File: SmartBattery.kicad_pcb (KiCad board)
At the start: 4 copper layers, 100 x 70 mm, 320 parts, among them J1 USB_C_Receptacle_USB2.0, J10 JST 2P-1.0, J11 JST 2P-1.0, J15 USB_C_Receptacle_USB2.0, J2 ST-USB-003A, J3 Barrel_Jack_MountingPin, J4 JST 2P-1.0, J5 JST 2P-1.0, J6 JST 2P-1.0, J7 JST 2P-1.0, J8 JST 2P-1.0, J9 JST 2P-1.0, Q1 VBA2625, Q10 AON7400A, Q11 AON7400A, Q12 AON7400A, Q13 AON7400A, Q14 2n7002K, Q15 VBA2625, Q16 VBA2625, Q17 VBA2625, Q18 VBA2625, Q19 VBA2625, Q2 2n7002K, Q20 VBA2625, Q21 2n7002K, Q22 VBA2625, Q23 2n7002K, Q24 VBA2625, Q3 AON7400A, Q4 AON7400A, Q5 AON7400A, Q6 AON7400A, Q7 2n7002K, Q8 AON7400A, Q9 AON7400A, SW1 SW_Push, SW2 SW_Push, U1 BQ25703ARSNR, U10 ESP32-WROOM-32U, U11 STUSB4500, U12 STUSB4700, U13 TPS2511DGNR, U2 BQ294706DSGR, U3 ITV4030, U4 BQ40Z50, U5 LM5175PWPR, U6 STM32F730R8T6, U7 W25Q128JVSIQ, U8 LMR14030SDDAR, U9 FS35ND01G-S1Y2QWFI000, Y1 Q13FC1350000400, Y2 Crystal_GND24

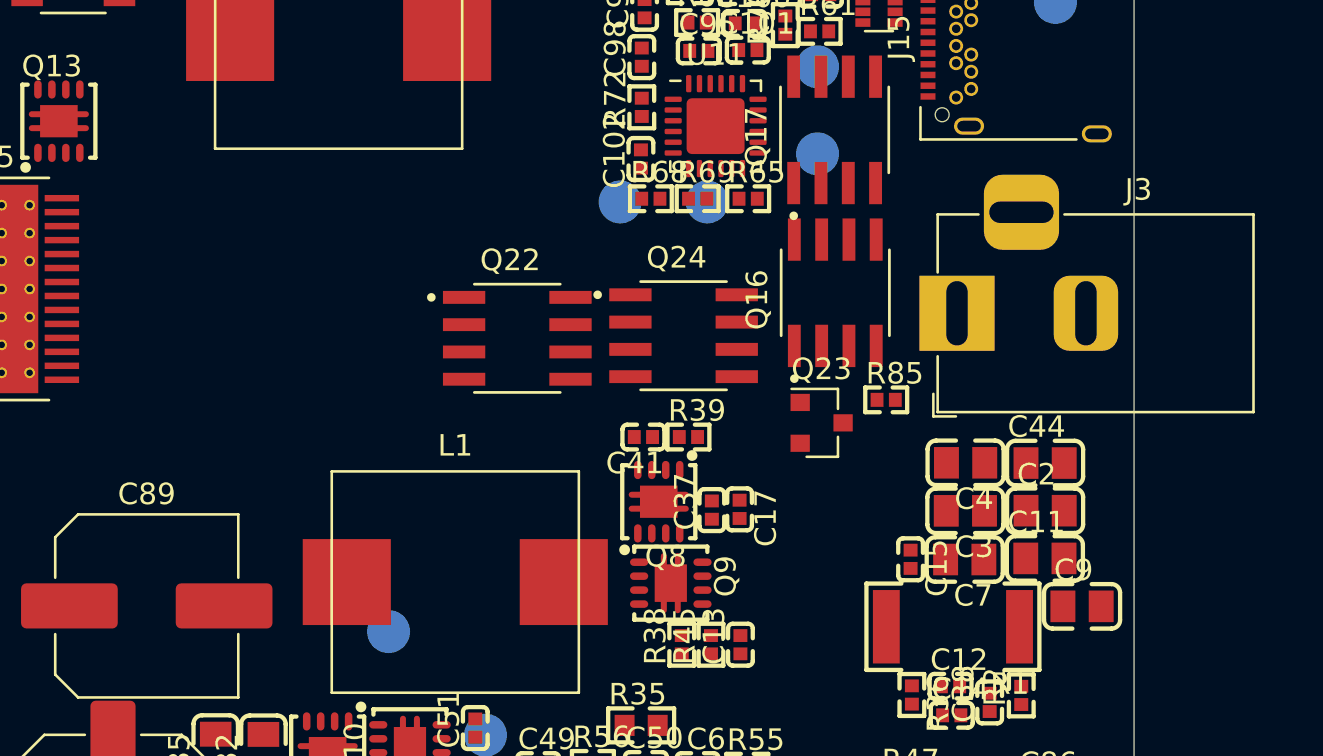
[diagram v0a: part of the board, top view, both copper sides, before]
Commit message: Added final touches to barrel jack and feedforward.
Need to finish output stage, then add screw terminals.
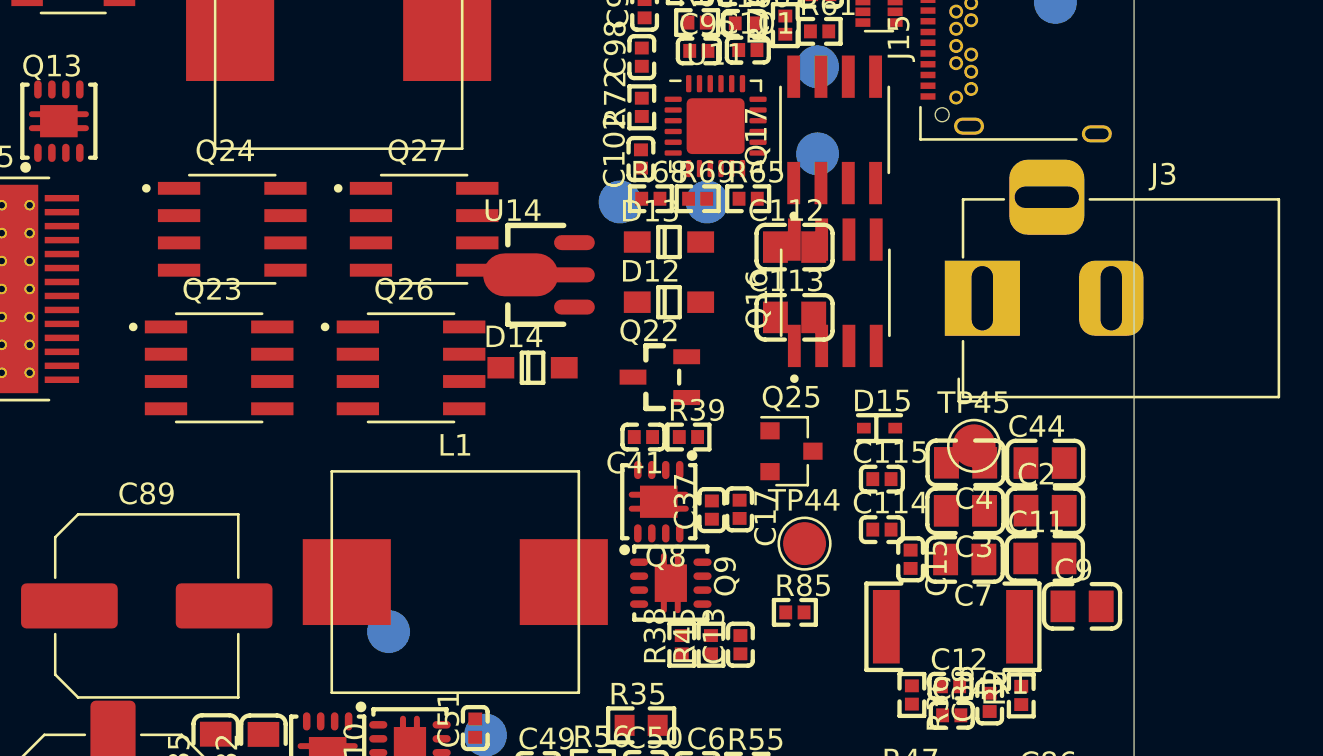
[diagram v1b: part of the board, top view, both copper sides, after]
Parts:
- added C112: 10u, lc_lib:0805_C, F.Cu at (84.2, 15.3)
- added C113: 10u, lc_lib:0805_C, F.Cu at (84.2, 18.6)
- added C114: 1uF 25v, lc_lib:0402_C, F.Cu at (88.3, 28.5)
- added C115: 1uF 25v, lc_lib:0402_C, F.Cu at (88.3, 26.1)
- added D12: B5817W-5819W, lc_lib:SOD-123, F.Cu at (78.4, 17.9)
- added D13: B5817W-5819W, lc_lib:SOD-123, F.Cu at (78.4, 15.1)
- added D14: B5817W-5819W, lc_lib:SOD-123, F.Cu at (72.0, 20.9)
- added D15: PESD24VS1UB-N, lc_lib:SOD-523, F.Cu at (88.2, 23.8)
- added Q25: 2n7002K, Package_TO_SOT_SMD:SOT-23, F.Cu at (84.1, 24.8)
- added Q26: VBA2625, SmartBattery:SOIC127P600X175-8N, F.Cu at (66.3, 20.9)
- added Q27: VBA2625, SmartBattery:SOIC127P600X175-8N, F.Cu at (67.0, 14.5)
- added TP44: TestPoint, TestPoint:TestPoint_Pad_D2.0mm, F.Cu at (84.7, 29.1)
- added TP45: TestPoint, TestPoint:TestPoint_Pad_D2.0mm, F.Cu at (92.6, 24.6)
- added U14: HT7533-1, lc_lib:SOT-89(SOT-89-3), F.Cu at (74.0, 16.6)
- Q22: value VBA2625 -> AO3401A; footprint SmartBattery:SOIC127P600X175-8N -> lc_lib:SOT-23(SOT-23-3)
- Q23: value 2n7002K -> VBA2625; footprint Package_TO_SOT_SMD:SOT-23 -> SmartBattery:SOIC127P600X175-8N
- moved Q23 28.2 mm to (57.4, 20.9)
- moved Q24 21.6 mm to (58.0, 14.5)
- moved R85 10.8 mm to (84.2, 32.3)
- moved Q22 6.88 mm to (77.9, 21.4)
- moved J3 1.37 mm to (92.9, 17.7)
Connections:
- J3 pad 1: /Charger/ADAPTER_IN -> /Barrel_Jack_Input/BARREL_RAW
- Q22 pad 2: Net-(Q22-Pad1) -> Net-(Q22-Pad2)
- Q22 pad 3: Net-(Q22-Pad1) -> Net-(Q22-Pad3)
- Q23 pad 2: Net-(Q23-Pad2) -> Net-(Q23-Pad1)
- Q23 pad 3: Net-(Q23-Pad3) -> Net-(Q23-Pad1)
- Q24 pad 1: Net-(Q24-Pad1) -> Net-(Q23-Pad1)
- Q24 pad 2: Net-(Q24-Pad1) -> Net-(Q23-Pad1)
- Q24 pad 3: Net-(Q24-Pad1) -> Net-(Q23-Pad1)
- Q24 pad 4: Net-(Q24-Pad4) -> Net-(Q23-Pad4)
- Q24 pad 5: Net-(Q24-Pad5) -> /Barrel_Jack_Input/BARREL_RAW
- Q24 pad 6: Net-(Q24-Pad5) -> /Barrel_Jack_Input/BARREL_RAW
- Q24 pad 7: Net-(Q24-Pad5) -> /Barrel_Jack_Input/BARREL_RAW
- Q24 pad 8: Net-(Q24-Pad5) -> /Barrel_Jack_Input/BARREL_RAW
- R85 pad 1: Net-(R85-Pad1) -> Net-(Q23-Pad1)
- R85 pad 2: Net-(R85-Pad2) -> Net-(Q23-Pad4)

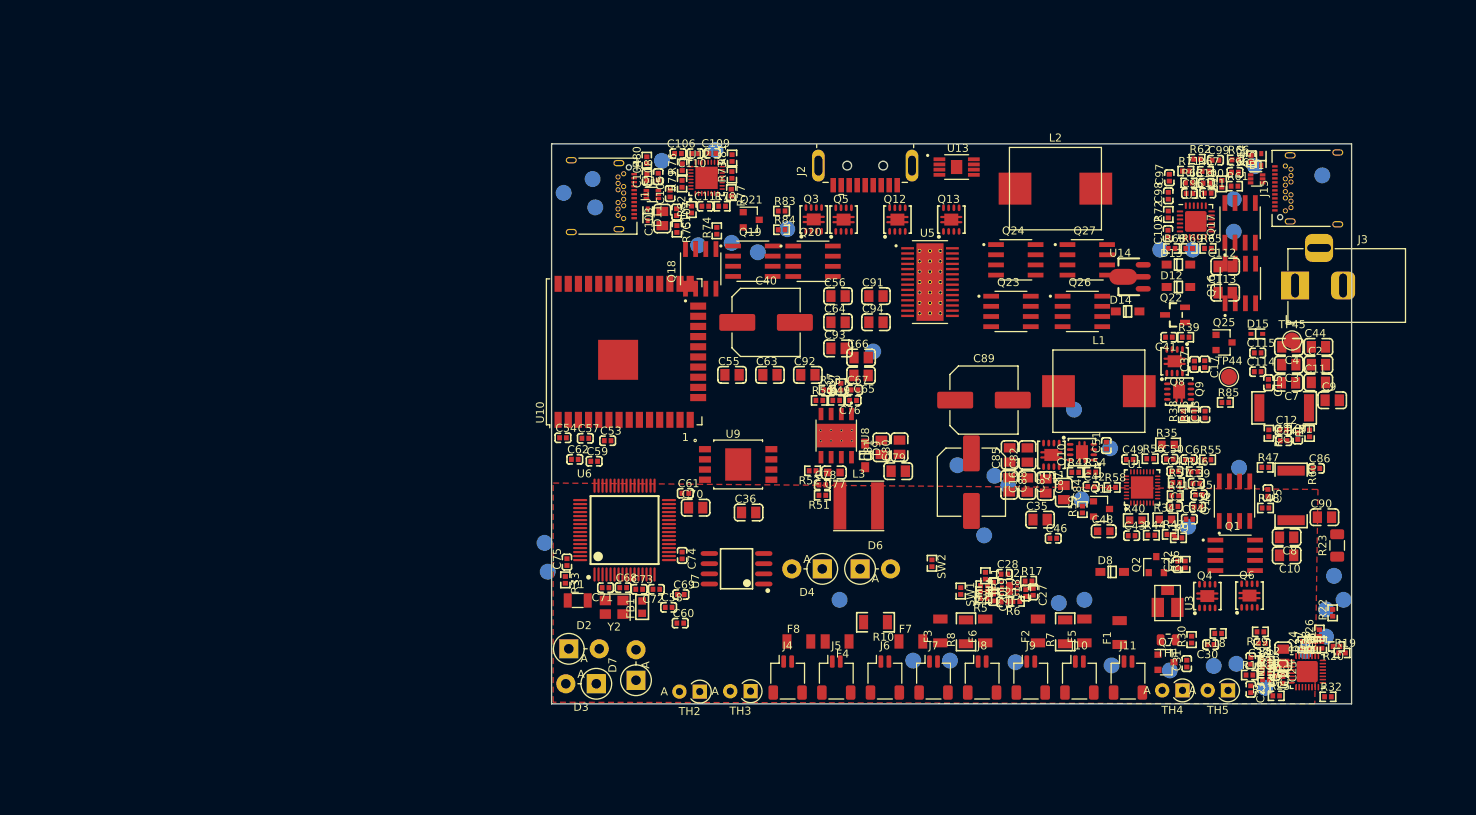
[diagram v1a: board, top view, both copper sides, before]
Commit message: Type_A_implemented. Sch "locked". PCB Layout started.
*Changelog:
*Type-a switching regulator (TBD -- need to check inductor,caps, stability. Maybe check both peripherial inductors?)
*Type-A load switch + connector + esd
*started layout..
*found out that my footprint for n fet is wrong. Fixing now, need to replace all of those.
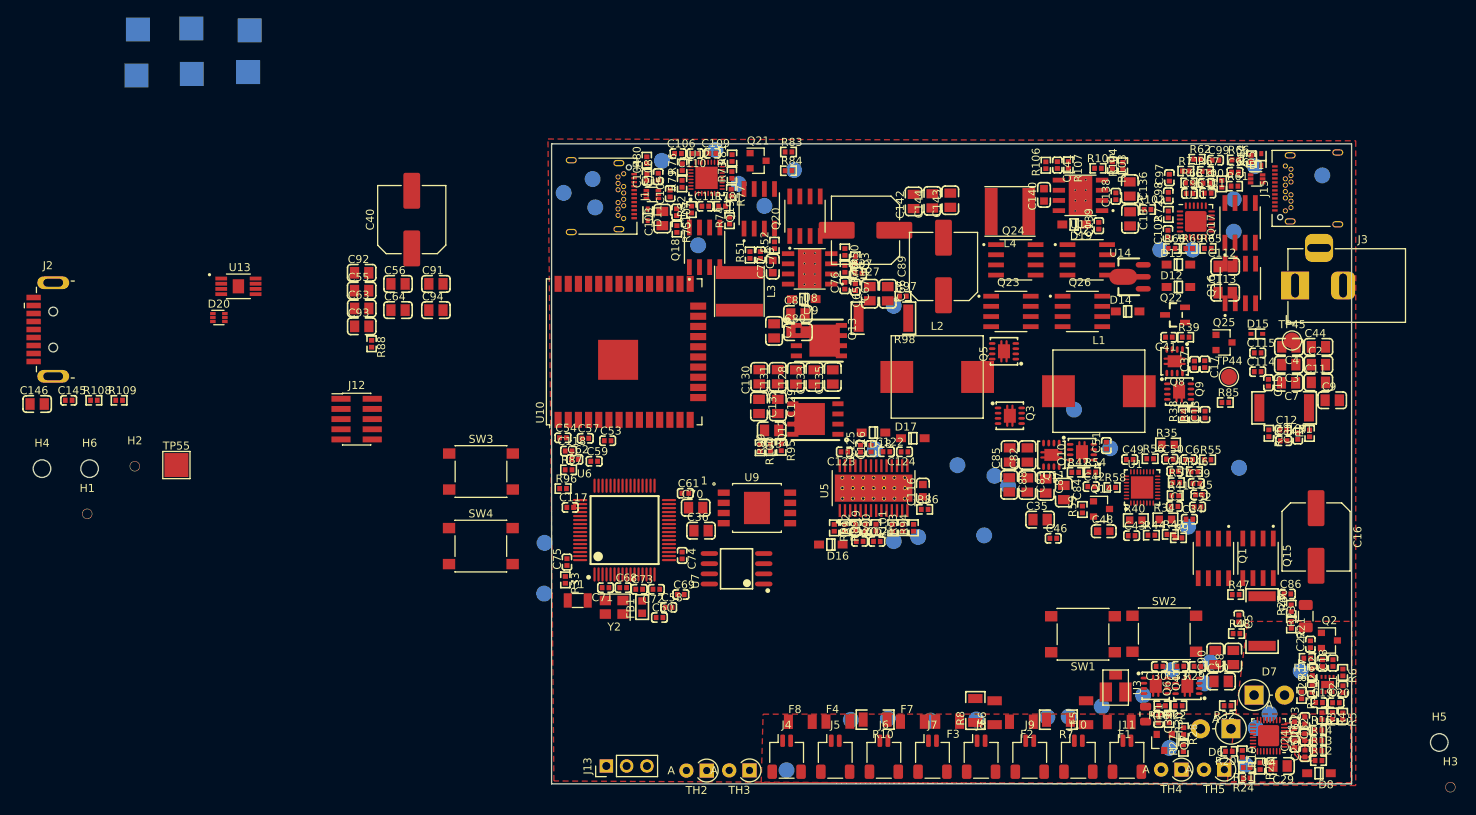
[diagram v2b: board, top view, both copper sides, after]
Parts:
- removed D2, D3, D4: LED, Diode_THT:D_DO-15_P3.81mm_Vertical_AnodeUp
- added C116: 4.7n, lc_lib:0603_C, F.Cu at (46.4, 43.4)
- added C117: 150pF, lc_lib:0402_C, F.Cu at (2.33, 45.4)
- added C118: 1uF 50v, lc_lib:0402_C, F.Cu at (2.13, 38.4)
- added C119: 47n, lc_lib:0402_C, F.Cu at (39.3, 48.0)
- added C120: 33n, lc_lib:0402_C, F.Cu at (38.5, 49.7)
- added C121: 68p, lc_lib:0402_C, F.Cu at (40.7, 49.7)
- added C122: 0.1uF, lc_lib:0402_C, F.Cu at (41.9, 38.5)
- added C123: 0.1uF, lc_lib:0402_C, F.Cu at (36.6, 38.5)
- added C124: 33nF, lc_lib:0402_C, F.Cu at (44.1, 38.5)
- added C125: 1uF 50v, lc_lib:0402_C, F.Cu at (38.6, 38.1)
- added C126: 1uF 50v, lc_lib:0402_C, F.Cu at (39.9, 38.1)
- added C127: 220u, Capacitor_SMD:C_Elec_8x10.2, F.Cu at (39.2, 10.8)
- added C128: 22u, lc_lib:0805_C, F.Cu at (30.5, 29.1)
- added C129: 22u, lc_lib:0805_C, F.Cu at (28.3, 32.8)
- added C130: 22u, lc_lib:0805_C, F.Cu at (26.0, 29.1)
- added C131: 22u, lc_lib:0805_C, F.Cu at (28.3, 29.1)
- added C132: 22u, lc_lib:0805_C, F.Cu at (25.9, 32.8)
- added C133: 22u, lc_lib:0805_C, F.Cu at (32.8, 29.1)
- added C134: 22u, lc_lib:0805_C, F.Cu at (27.5, 35.8)
- added C135: 22u, lc_lib:0805_C, F.Cu at (35.1, 29.1)
- added C136: 10u, lc_lib:0805_C, F.Cu at (72.3, 5.65)
- added C137: 10u, lc_lib:0805_C, F.Cu at (72.3, 9.38)
- added C138: 0.1u 25v, lc_lib:0402_C, F.Cu at (70.5, 6.55)
- added C139: 0.1u 25v, lc_lib:0402_C, F.Cu at (68.4, 10.2)
- added C140: 8.2nF, lc_lib:0603_C, F.Cu at (61.5, 6.38)
- added C141: 220pF, lc_lib:0402_C, F.Cu at (63.2, 2.65)
- added C142: 22u, lc_lib:0805_C, F.Cu at (45.2, 7.20)
- added C143: 22u, lc_lib:0805_C, F.Cu at (49.8, 7.05)
- added C144: 22u, lc_lib:0805_C, F.Cu at (47.6, 7.13)
- added C145: 0.1uF 25v, lc_lib:0402_C, F.Cu at (-60.4, 32.1)
- added C146: 22u, lc_lib:0805_C, F.Cu at (-64.3, 32.5)
- added D16: B5817W-5819W, lc_lib:SOD-123, F.Cu at (34.9, 50.1)
- added D17: B5817W-5819W, lc_lib:SOD-123, F.Cu at (45.2, 36.8)
- added D18: B5817W-5819W, lc_lib:SOD-123, F.Cu at (40.2, 36.1)
- added D19: B5817W-5819W, lc_lib:SOD-123, F.Cu at (65.3, 10.1)
- added D20: ESDA6V8AV6, Package_TO_SOT_SMD:SOT-563, F.Cu at (-41.6, 21.7)
- added H1: MountingHole, SmartBattery:MountingHole_1.152mm_JLPCB, F.Cu at (-58.0, 46.2)
- added H2: MountingHole, SmartBattery:MountingHole_1.152mm_JLPCB, F.Cu at (-52.1, 40.3)
- added H3: MountingHole, SmartBattery:MountingHole_1.152mm_JLPCB, F.Cu at (112.3, 80.4)
- added H4: MountingHole, MountingHole:MountingHole_2.2mm_M2, F.Cu at (-63.7, 40.6)
- added H5: MountingHole, MountingHole:MountingHole_2.2mm_M2, F.Cu at (111.0, 74.8)
- added H6: MountingHole, MountingHole:MountingHole_2.2mm_M2, F.Cu at (-57.8, 40.6)
- added J12: Conn_01x10_Male, Connector_PinHeader_1.27mm:PinHeader_2x05_P1.27mm_Vertical_SMD, F.Cu at (-24.4, 34.4)
- added J13: Conn_01x03_Male, Connector_PinHeader_2.54mm:PinHeader_1x03_P2.54mm_Vertical, F.Cu at (6.84, 77.8)
- added L4: 6.8uH 47mO SWPA6028S6R8MT, Inductor_SMD:L_Taiyo-Yuden_NR-60xx, F.Cu at (57.3, 8.45)
- added R100: ??, lc_lib:0402_R, F.Cu at (26.1, 38.0)
- added R101: ??, lc_lib:0402_R, F.Cu at (42.6, 48.0)
- added R102: 0, lc_lib:0402_R, F.Cu at (74.5, 8.21)
- added R103: 0, lc_lib:0402_R, F.Cu at (70.1, 2.69)
- added R104: ??, lc_lib:0402_R, F.Cu at (71.4, 2.75)
- added R105: 20k, lc_lib:0402_R, F.Cu at (68.3, 3.06)
- added R106: ???, lc_lib:0402_R, F.Cu at (61.8, 2.67)
- added R107: 15k, lc_lib:0402_R, F.Cu at (64.6, 2.63)
- added R108: 100k, lc_lib:0402_R, F.Cu at (-57.2, 32.1)
- added R109: 22.1k, lc_lib:0402_R, F.Cu at (-54.1, 32.1)
- added R86: 10k, lc_lib:0402_R, F.Cu at (46.6, 45.7)
- added R87: ??, lc_lib:0402_R, F.Cu at (2.13, 40.7)
- added R88: ??, lc_lib:0402_R, F.Cu at (-22.5, 25.0)
- added R89: ??, lc_lib:0402_R, F.Cu at (36.7, 48.0)
- added R90: 68.1k, lc_lib:0402_R, F.Cu at (40.5, 48.0)
- added R91: ??, lc_lib:0402_R, F.Cu at (35.3, 48.0)
- added R92: 93.1k, lc_lib:0402_R, F.Cu at (38.0, 48.0)
- added R93: 0, lc_lib:0402_R, F.Cu at (43.9, 48.0)
- added R94: 0, lc_lib:0402_R, F.Cu at (45.2, 48.0)
- added R95: 0, lc_lib:0402_R, F.Cu at (28.7, 37.9)
- added R96: 1, lc_lib:0402_R, F.Cu at (1.44, 43.1)
- added R97: 1, lc_lib:0402_R, F.Cu at (43.9, 19.0)
- added R98: 0.01, lc_lib:2512_R, F.Cu at (41.5, 21.8)
- added R99: ??, lc_lib:0402_R, F.Cu at (27.4, 38.0)
- added SW3: SW_Push, Button_Switch_SMD:SW_Push_1P1T_NO_6x6mm_H9.5mm, F.Cu at (-8.82, 41.0)
- added SW4: SW_Push, Button_Switch_SMD:SW_Push_1P1T_NO_6x6mm_H9.5mm, F.Cu at (-8.85, 50.3)
- added TP46: TestPoint_Flag, TestPoint:TestPoint_Pad_3.0x3.0mm, B.Cu at (-51.9, -8.55)
- added TP47: TestPoint_Flag, TestPoint:TestPoint_Pad_3.0x3.0mm, B.Cu at (-37.7, -14.2)
- added TP48: TestPoint_Flag, TestPoint:TestPoint_Pad_3.0x3.0mm, B.Cu at (-37.9, -8.97)
- added TP49: TestPoint_Flag, TestPoint:TestPoint_Pad_3.0x3.0mm, B.Cu at (-45.0, -14.4)
- added TP50: TestPoint_Flag, TestPoint:TestPoint_Pad_3.0x3.0mm, B.Cu at (-51.7, -14.3)
- added TP51: TestPoint_Flag, TestPoint:TestPoint_Pad_3.0x3.0mm, B.Cu at (-45.0, -8.74)
- added TP52: TestPoint, TestPoint:TestPoint_Pad_D2.0mm, B.Cu at (42.8, 49.7)
- added TP53: TestPoint, TestPoint:TestPoint_Pad_D2.0mm, B.Cu at (45.8, 49.1)
- added TP54: TestPoint, TestPoint:TestPoint_Pad_D2.0mm, B.Cu at (40.4, 38.2)
- added TP55: TestPoint_Flag, TestPoint:TestPoint_Pad_3.0x3.0mm, F.Cu at (-46.9, 40.1)
- added U15: LMR14030SDDAR, SmartBattery:NOPB, F.Cu at (66.1, 6.44)
- L2: value MWSA0603-2R2MT -> MWSA1004-2R2MT
- Q12, Q13: value AON7400A -> BSC067N06LS3; footprint lc_lib:QFN-8_3X3X065P -> lc_lib:DFN-8_5X6MM
- SW1, SW2: footprint lc_lib:0402_R -> Button_Switch_SMD:SW_Push_1P1T_NO_6x6mm_H9.5mm
- moved J2 104.1 mm to (-63.0, 23.2), turned to 0 degrees
- moved U13 91.0 mm to (-39.1, 17.8)
- moved D7 77.3 mm to (87.8, 68.9), turned to 0 degrees
- moved C93 59.6 mm to (-23.7, 22.8)
- moved TP5 57.8 mm to (29.4, 78.3)
- moved C92 57.2 mm to (-23.7, 16.1)
- moved C56 55.0 mm to (-19.2, 17.5)
- moved C64 55.0 mm to (-19.2, 20.8)
- moved C91 55.0 mm to (-14.5, 17.5)
- moved C94 55.0 mm to (-14.5, 20.8)
- moved C63 51.7 mm to (-23.7, 20.6)
- moved D6 50.5 mm to (84.9, 73.1), turned to 180 degrees
- moved C55 47.5 mm to (-23.7, 18.4)
- moved R5 47.3 mm to (98.9, 71.6), turned to 270 degrees
- moved R4 46.3 mm to (97.6, 71.5), turned to 270 degrees
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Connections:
- net Net-(U13-Pad4) renamed /Output_TYPEA/OUTPUT_CS_N
- net Net-(U5-Pad17) renamed /OutputStage/PGOOD
- net Net-(U6-Pad27) renamed /MCU/QUADSPI_CLK
- net Net-(U6-Pad40) renamed /MCU/QUADSPI_BK1_IO0
- net Net-(U6-Pad51) renamed /MCU/QUADSPI_BK1_IO1
- net Net-(U6-Pad52) renamed /MCU/QUADSPI_BK2_NCS
- net Net-(U6-Pad58) renamed /MCU/QUASPI_BK1_NCS
- D9 pad 1: Net-(D9-Pad1) -> /Peripheral_3p3v/3p3_SWITCHED_NODE
- J2 pad 1: Net-(J2-Pad1) -> Net-(C146-Pad1)
- J2 pad 2: Net-(J2-Pad2) -> Net-(D20-Pad6)
- J2 pad 3: Net-(J2-Pad3) -> Net-(D20-Pad3)
- J2 pad 4: Net-(J2-Pad4) -> GND
- J2 pad 5: Net-(J2-Pad5) -> GND
- L2 pad 1: Net-(L2-Pad1) -> /OutputStage/SW2
- L2 pad 2: Net-(L2-Pad2) -> /OutputStage/SW1
- Q12 pad 1: Net-(Q12-Pad1) -> /OutputStage/SW2
- Q12 pad 2: Net-(Q12-Pad1) -> /OutputStage/SW2
- Q12 pad 3: Net-(Q12-Pad1) -> /OutputStage/SW2
- Q12 pad 4: Net-(Q12-Pad4) -> /OutputStage/HDRV_2
- Q12 pad 5: Net-(Q12-Pad5) -> /Type_C_Output/OUTPUT_TYPEC_PWR
- Q12 pad 6: Net-(Q12-Pad5) -> /Type_C_Output/OUTPUT_TYPEC_PWR
- Q12 pad 7: Net-(Q12-Pad5) -> /Type_C_Output/OUTPUT_TYPEC_PWR
- Q12 pad 8: Net-(Q12-Pad5) -> /Type_C_Output/OUTPUT_TYPEC_PWR
- Q13 pad 4: Net-(Q13-Pad4) -> /OutputStage/LDRV_2
- Q13 pad 5: Net-(Q13-Pad5) -> /OutputStage/SW2
- Q13 pad 6: Net-(Q13-Pad5) -> /OutputStage/SW2
- Q13 pad 7: Net-(Q13-Pad5) -> /OutputStage/SW2
- Q13 pad 8: Net-(Q13-Pad5) -> /OutputStage/SW2
- Q3 pad 1: Net-(Q3-Pad1) -> /OutputStage/SW1
- Q3 pad 2: Net-(Q3-Pad1) -> /OutputStage/SW1
- Q3 pad 3: Net-(Q3-Pad1) -> /OutputStage/SW1
- Q3 pad 4: Net-(Q3-Pad4) -> /OutputStage/HDRV_1
- Q3 pad 5: Net-(Q3-Pad5) -> /Charger/VSYS
- Q3 pad 6: Net-(Q3-Pad5) -> /Charger/VSYS
- Q3 pad 7: Net-(Q3-Pad5) -> /Charger/VSYS
- Q3 pad 8: Net-(Q3-Pad5) -> /Charger/VSYS
- Q5 pad 1: Net-(Q5-Pad1) -> Net-(Q13-Pad1)
- Q5 pad 2: Net-(Q5-Pad1) -> Net-(Q13-Pad1)
- Q5 pad 3: Net-(Q5-Pad1) -> Net-(Q13-Pad1)
- Q5 pad 4: Net-(Q5-Pad4) -> /OutputStage/LDRV_1
- Q5 pad 5: Net-(Q5-Pad5) -> /OutputStage/SW1
- Q5 pad 6: Net-(Q5-Pad5) -> /OutputStage/SW1
- Q5 pad 7: Net-(Q5-Pad5) -> /OutputStage/SW1
- Q5 pad 8: Net-(Q5-Pad5) -> /OutputStage/SW1
- U13 pad 1: Net-(U13-Pad1) -> GND
- U13 pad 3: Net-(U13-Pad3) -> /Peripheral_3p3v/5v0
- U13 pad 5: Net-(U13-Pad5) -> /Output_TYPEA/5v_ENABLE
- U13 pad 6: Net-(U13-Pad6) -> Net-(D20-Pad3)
- U13 pad 7: Net-(U13-Pad7) -> Net-(D20-Pad6)
- U13 pad 8: Net-(U13-Pad8) -> Net-(C146-Pad1)
- U13 pad 9: Net-(U13-Pad9) -> GND
- U5 pad 10: Net-(U5-Pad10) -> GND
- U5 pad 12: Net-(U5-Pad12) -> /Type_C_Output/OUTPUT_TYPEC_PWR
- U5 pad 18: Net-(U5-Pad18) -> /OutputStage/SW2
- U5 pad 19: Net-(U5-Pad19) -> /OutputStage/HDRV_2
- U5 pad 21: Net-(U5-Pad21) -> /OutputStage/LDRV_2
- U5 pad 22: Net-(U5-Pad22) -> GND
- U5 pad 25: Net-(U5-Pad25) -> /OutputStage/LDRV_1
- U5 pad 27: Net-(U5-Pad27) -> /OutputStage/HDRV_1
- U5 pad 28: Net-(U5-Pad28) -> /OutputStage/SW1
- U5 pad 29: Net-(U5-Pad29) -> GND
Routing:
- net Net-(C24-Pad2): track 0.00 -> 6.03 mm
- net Net-(C25-Pad2): track 0.00 -> 5.31 mm
- net Net-(C24-Pad1): track 0.00 -> 5.29 mm
- net Net-(C23-Pad1): track 0.00 -> 4.08 mm
- net Net-(C32-Pad2): track 0.00 -> 1.43 mm
- net Net-(C32-Pad1): track 0.00 -> 1.26 mm
- net BAT_VN_0: track 0.00 -> 0.67 mm, vias 0 -> 1
- added copper zone on F.Cu, net GND
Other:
- board size 100 x 70 mm -> 100 x 80 mm

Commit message: Much layout. Wow
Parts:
- Q10, Q11, Q3, Q4, Q5, Q6, Q9: value AON7400A -> AON7400A; footprint lc_lib:QFN-8_3X3X065P -> lc_lib:SON-8_3.3X3.3MM
- TP44, TP45: moved to B.Cu
- moved TP38 52.4 mm to (55.2, 40.0)
- moved J12 44.5 mm to (7.14, 65.8)
- moved Q9 17.8 mm to (62.1, 38.1), turned to 0 degrees
- moved Q11 17.5 mm to (77.9, 30.6), turned to 90 degrees
- moved Q3 8.76 mm to (56.7, 25.2), turned to 90 degrees
- moved Q5 8.00 mm to (57.2, 33.9)
- moved TP15 5.82 mm to (84.2, 69.6)
- moved TP16 4.67 mm to (92.6, 74.0)
- moved R32 3.66 mm to (80.8, 70.3)
- moved TP45 2.19 mm to (93.1, 22.4)
- moved TP1 1.74 mm to (58.8, 42.8)
- moved TP21 1.74 mm to (54.3, 42.9)
- moved H3 1.22 mm to (111.3, 79.9)
- moved C10 1.14 mm to (83.4, 68.3), turned to 270 degrees
- moved C117 1.12 mm to (1.21, 45.5), turned to 90 degrees
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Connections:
- Q10 pad 1: GND -> Net-(Q10-Pad1)
- Q10 pad 2: GND -> Net-(Q10-Pad1)
- Q10 pad 3: GND -> Net-(Q10-Pad1)
- Q10 pad 4: Net-(C51-Pad2) -> Net-(Q10-Pad4)
- U2 pad 9: (no net) -> BAT_VN_0
- U4 pad 33: (no net) -> BAT_VN_0
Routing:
- net BAT_VP_0: track 0.00 -> 92.5 mm, vias 0 -> 3
- net BAT_VP_3: track 0.00 -> 64.7 mm, vias 0 -> 5
- net BAT_VP_1: track 0.00 -> 64.4 mm, vias 0 -> 2
- net BAT_VP_2: track 0.00 -> 58.7 mm, vias 0 -> 3
- net BAT_VN_0: track 0.67 -> 54.7 mm, vias 1 -> 43
- net Net-(TH4-Pad2): track 0.00 -> 48.6 mm, vias 0 -> 1
- net Net-(C31-Pad2): track 0.00 -> 36.4 mm, vias 0 -> 5
- net Net-(Q4-Pad5): track 0.00 -> 31.2 mm, vias 0 -> 2
- net /Battery connection and protection/BATT_PACK_P: track 0.00 -> 29.1 mm
- net Net-(C5-Pad1): track 0.00 -> 23.7 mm
- net Net-(TH5-Pad2): track 0.00 -> 18.0 mm, vias 0 -> 1
- net BAT_VN_3: track 0.00 -> 11.8 mm
- net Net-(C30-Pad2): track 0.00 -> 11.6 mm
- net BAT_VN_2: track 0.00 -> 11.2 mm
- net BAT_VN_1: track 0.00 -> 11.0 mm
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- added copper zone on B.Cu, net BAT_VN_0
- added copper zone on In1.Cu, net BAT_VN_0
- added copper zone on In2.Cu, net BAT_VN_0
- added copper zone on B.Cu, net GND
- added copper zone on In1.Cu, net GND
- added copper zone on In2.Cu, net GND
